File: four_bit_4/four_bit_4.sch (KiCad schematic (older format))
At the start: 1 part, among them P1 DIN_41612_128P

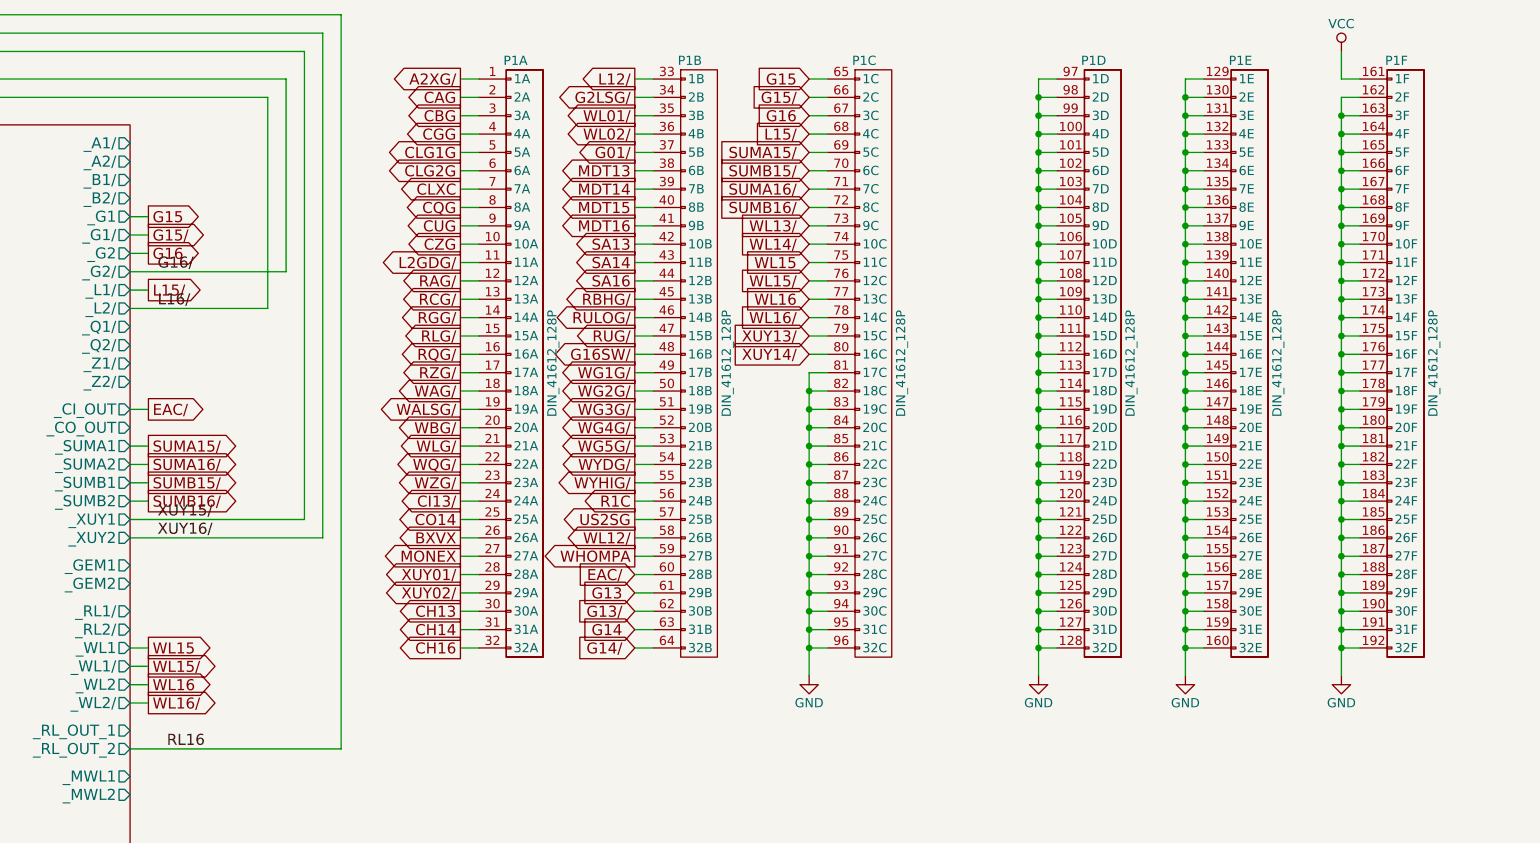
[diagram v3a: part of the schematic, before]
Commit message: Corrected a couple of bugs found by Quartus (L16/, Z15/, Z16/ not connected)
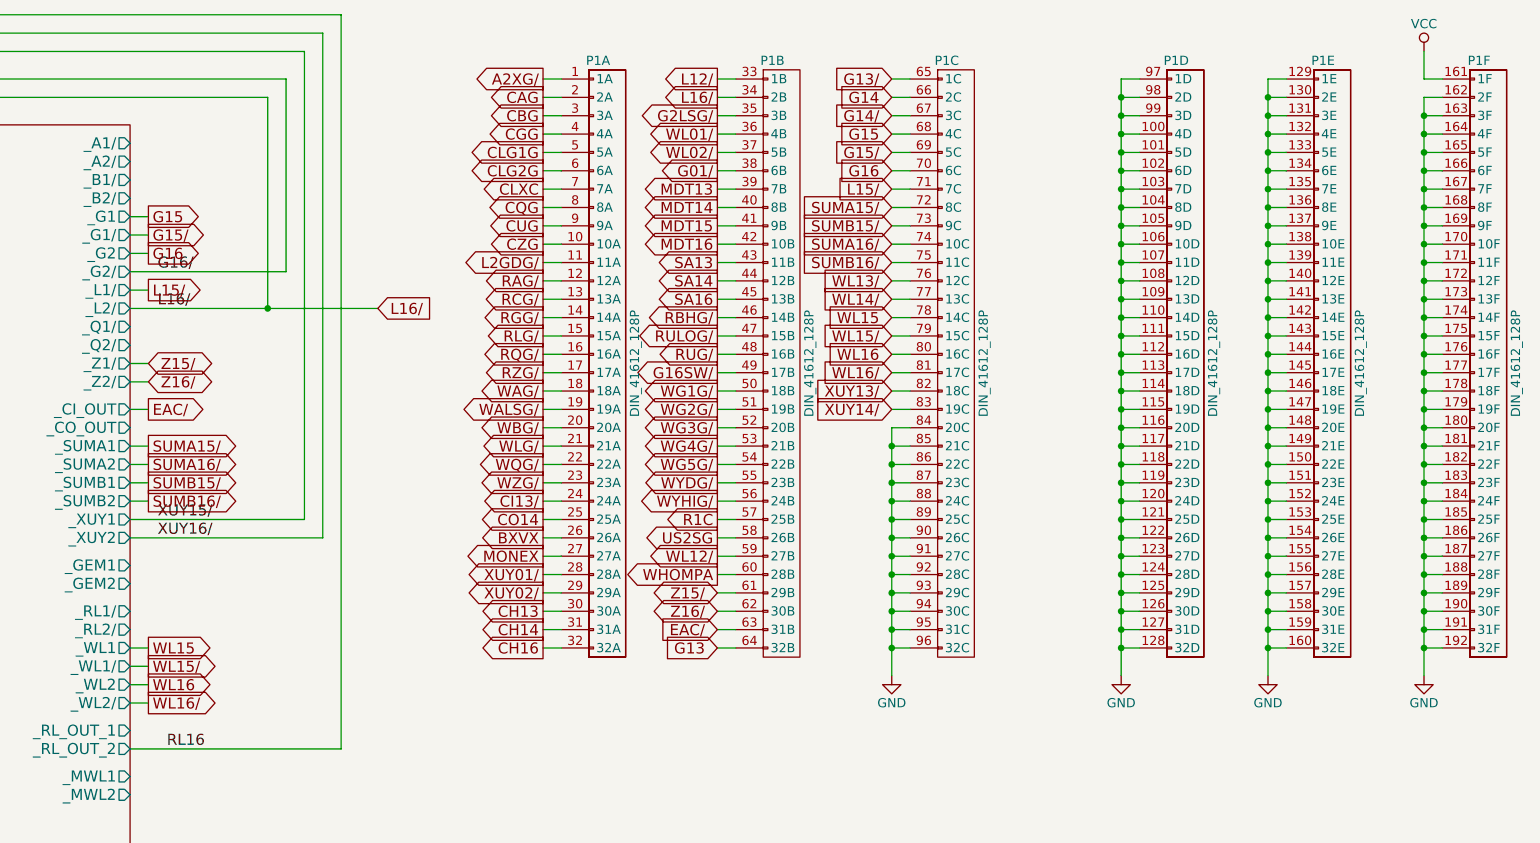
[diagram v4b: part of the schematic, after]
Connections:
- net EAC/: now also P1.63 (31B); no longer P1.60 (28B)
- net G01/: now also P1.38 (6B); no longer P1.37 (5B)
- net G13: now also P1.64 (32B); no longer P1.61 (29B)
- net G13/: now also P1.65 (1C); no longer P1.62 (30B)
- net G14: now also P1.66 (2C); no longer P1.63 (31B)
- net G14/: now also P1.67 (3C); no longer P1.64 (32B)
- net G15: now also P1.68 (4C); no longer P1.65 (1C)
- net G15/: now also P1.69 (5C); no longer P1.66 (2C)
- net G16: now also P1.70 (6C); no longer P1.67 (3C)
- net G16SW/: now also P1.49 (17B); no longer P1.48 (16B)
- net G2LSG/: now also P1.35 (3B); no longer P1.34 (2B)
- net GND: no longer P1.81 (17C), P1.82 (18C), P1.83 (19C)
- net L15/: now also P1.71 (7C); no longer P1.68 (4C)
- net L16/: now also P1.34 (2B)
- net MDT13: now also P1.39 (7B); no longer P1.38 (6B)
- net MDT14: now also P1.40 (8B); no longer P1.39 (7B)
- net MDT15: now also P1.41 (9B); no longer P1.40 (8B)
- net MDT16: now also P1.42 (10B); no longer P1.41 (9B)
- net R1C: now also P1.57 (25B); no longer P1.56 (24B)
- net RBHG/: now also P1.46 (14B); no longer P1.45 (13B)
- net RUG/: now also P1.48 (16B); no longer P1.47 (15B)
- net RULOG/: now also P1.47 (15B); no longer P1.46 (14B)
- net SA13: now also P1.43 (11B); no longer P1.42 (10B)
- net SA14: now also P1.44 (12B); no longer P1.43 (11B)
- net SA16: now also P1.45 (13B); no longer P1.44 (12B)
- net SUMA15/: now also P1.72 (8C); no longer P1.69 (5C)
- net SUMA16/: now also P1.74 (10C); no longer P1.71 (7C)
- net SUMB15/: now also P1.73 (9C); no longer P1.70 (6C)
- net SUMB16/: now also P1.75 (11C); no longer P1.72 (8C)
- net US2SG: now also P1.58 (26B); no longer P1.57 (25B)
- net WG1G/: now also P1.50 (18B); no longer P1.49 (17B)
- net WG2G/: now also P1.51 (19B); no longer P1.50 (18B)
- net WG3G/: now also P1.52 (20B); no longer P1.51 (19B)
- net WG4G/: now also P1.53 (21B); no longer P1.52 (20B)
- net WG5G/: now also P1.54 (22B); no longer P1.53 (21B)
- net WHOMPA: now also P1.60 (28B); no longer P1.59 (27B)
- net WL01/: now also P1.36 (4B); no longer P1.35 (3B)
- net WL02/: now also P1.37 (5B); no longer P1.36 (4B)
- net WL12/: now also P1.59 (27B); no longer P1.58 (26B)
- net WL13/: now also P1.76 (12C); no longer P1.73 (9C)
- net WL14/: now also P1.77 (13C); no longer P1.74 (10C)
- net WL15: now also P1.78 (14C); no longer P1.75 (11C)
- net WL15/: now also P1.79 (15C); no longer P1.76 (12C)
- net WL16: now also P1.80 (16C); no longer P1.77 (13C)
- net WL16/: now also P1.81 (17C); no longer P1.78 (14C)
- net WYDG/: now also P1.55 (23B); no longer P1.54 (22B)
- net WYHIG/: now also P1.56 (24B); no longer P1.55 (23B)
- net XUY13/: now also P1.82 (18C); no longer P1.79 (15C)
- net XUY14/: now also P1.83 (19C); no longer P1.80 (16C)
- new net Z15/: P1.61 (29B)
- new net Z16/: P1.62 (30B)
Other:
- moved on the sheet: P1A, P1B, P1C, P1D, P1E, P1F

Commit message: Added and tied in module 15, the rupt service (and banking/rope+strand selection)
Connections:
- net GND: no longer P1.84 (20C), P1.85 (21C), P1.86 (22C), P1.87 (23C), P1.88 (24C), P1.89 (25C), P1.90 (26C), P1.91 (27C)
- net SUMA15/: now also P1.80 (16C); no longer P1.72 (8C)
- net SUMA16/: now also P1.82 (18C); no longer P1.74 (10C)
- net SUMB15/: now also P1.81 (17C); no longer P1.73 (9C)
- net SUMB16/: now also P1.83 (19C); no longer P1.75 (11C)
- net WL13/: now also P1.84 (20C); no longer P1.76 (12C)
- net WL14/: now also P1.85 (21C); no longer P1.77 (13C)
- net WL15: now also P1.86 (22C); no longer P1.78 (14C)
- net WL15/: now also P1.87 (23C); no longer P1.79 (15C)
- net WL16: now also P1.88 (24C); no longer P1.80 (16C)
- net WL16/: now also P1.89 (25C); no longer P1.81 (17C)
- net XUY13/: now also P1.90 (26C); no longer P1.82 (18C)
- net XUY14/: now also P1.91 (27C); no longer P1.83 (19C)
- new net RL13/: P1.72 (8C)
- new net RL14/: P1.73 (9C)
- new net RL15/: P1.74 (10C)
- new net RL16/: P1.75 (11C)
- new net SUMA13/: P1.76 (12C)
- new net SUMA14/: P1.78 (14C)
- new net SUMB13/: P1.77 (13C)
- new net SUMB14/: P1.79 (15C)
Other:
- moved on the sheet: P1C
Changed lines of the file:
@@
 L DIN_41612_128P P1
 U 3 1 568CD52A
-P 10450 2500
-F 0 "P1" H 10450 4150 50  0000 C CNN
-F 1 "DIN_41612_128P" V 10650 2500 50  0000 C CNN
-F 2 "" H 10450 2500 60  0000 C CNN
-F 3 "" H 10450 2500 60  0000 C CNN
-	3    10450 2500
+P 10550 2500
+F 0 "P1" H 10550 4150 50  0000 C CNN
+F 1 "DIN_41612_128P" V 10750 2500 50  0000 C CNN
+F 2 "" H 10550 2500 60  0000 C CNN
+F 3 "" H 10550 2500 60  0000 C CNN
+	3    10550 2500
 	1    0    0    -1
 $EndComp
@@
 L GND #PWR07
 U 1 1 568CD535
-P 10150 4200
-F 0 "#PWR07" H 10150 3950 50  0001 C CNN
-F 1 "GND" H 10150 4050 50  0000 C CNN
-F 2 "" H 10150 4200 60  0000 C CNN
-F 3 "" H 10150 4200 60  0000 C CNN
-	1    10150 4200
+P 10250 4200
+F 0 "#PWR07" H 10250 3950 50  0001 C CNN
+F 1 "GND" H 10250 4050 50  0000 C CNN
+F 2 "" H 10250 4200 60  0000 C CNN
+F 3 "" H 10250 4200 60  0000 C CNN
+	1    10250 4200
 	1    0    0    -1
 $EndComp
@@
 	4600 8350 4500 8350
 Wire Wire Line
-	10150 2850 10250 2850
-Wire Wire Line
-	10150 2950 10250 2950
-Connection ~ 10150 2950
-Wire Wire Line
-	10150 3050 10250 3050
-Connection ~ 10150 3050
-Wire Wire Line
-	10150 3150 10250 3150
-Connection ~ 10150 3150
-Wire Wire Line
-	10150 3250 10250 3250
-Connection ~ 10150 3250
-Wire Wire Line
-	10150 3350 10250 3350
-Connection ~ 10150 3350
-Wire Wire Line
-	10150 3450 10250 3450
-Connection ~ 10150 3450
-Wire Wire Line
-	10150 3550 10250 3550
-Connection ~ 10150 3550
-Wire Wire Line
-	10150 3650 10250 3650
-Connection ~ 10150 3650
-Wire Wire Line
-	10150 3750 10250 3750
-Connection ~ 10150 3750
-Wire Wire Line
-	10150 3850 10250 3850
-Connection ~ 10150 3850
-Wire Wire Line
-	10150 3950 10250 3950
-Connection ~ 10150 3950
-Wire Wire Line
-	10150 4050 10250 4050
-Connection ~ 10150 4050
+	10250 3650 10350 3650
+Wire Wire Line
+	10250 3750 10350 3750
+Connection ~ 10250 3750
+Wire Wire Line
+	10250 3850 10350 3850
+Connection ~ 10250 3850
+Wire Wire Line
+	10250 3950 10350 3950
+Connection ~ 10250 3950
+Wire Wire Line
+	10250 4050 10350 4050
+Connection ~ 10250 4050
 Wire Wire Line
 	6000 2000 6850 2000
@@
 Wire Wire Line
 	6000 1800 6100 1800
-Text GLabel 10150 950  0    60   Input ~ 0
+Text GLabel 10250 950  0    60   Input ~ 0
 G13/
 Wire Wire Line
-	10250 950  10150 950
-Text GLabel 10150 1150 0    60   Input ~ 0
+	10350 950  10250 950
+Text GLabel 10250 1150 0    60   Input ~ 0
 G14/
 Wire Wire Line
-	10250 1150 10150 1150
-Text GLabel 10150 1350 0    60   Input ~ 0
+	10350 1150 10250 1150
+Text GLabel 10250 1350 0    60   Input ~ 0
 G15/
 Wire Wire Line
-	10250 1350 10150 1350
+	10350 1350 10250 1350
 Text GLabel 6100 2100 2    60   Output ~ 0
 L15/
 Wire Wire Line
 	6000 2100 6100 2100
-Text GLabel 10150 1550 0    60   Input ~ 0
+Text GLabel 10250 1550 0    60   Input ~ 0
 L15/
 Wire Wire Line
-	10250 1550 10150 1550
+	10350 1550 10250 1550
 Text GLabel 6100 3050 2    60   Output ~ 0
 SUMA16/
@@
 Wire Wire Line
 	6000 3250 6100 3250
-Text GLabel 10150 1850 0    60   Input ~ 0
+Text GLabel 10250 2650 0    60   Input ~ 0
 SUMA16/
 Wire Wire Line
-	10250 1850 10150 1850
-Text GLabel 10150 1950 0    60   Input ~ 0
+	10350 2650 10250 2650
+Text GLabel 10250 2750 0    60   Input ~ 0
 SUMB16/
 Wire Wire Line
-	10250 1950 10150 1950
+	10350 2750 10250 2750
 Text GLabel 3250 3350 2    60   Output ~ 0
 XUY13/
@@
 Wire Wire Line
 	3150 3450 3250 3450
-Text GLabel 10150 2650 0    60   Input ~ 0
+Text GLabel 10250 3450 0    60   Input ~ 0
 XUY13/
 Wire Wire Line
-	10250 2650 10150 2650
-Text GLabel 10150 2750 0    60   Input ~ 0
+	10350 3450 10250 3450
+Text GLabel 10250 3550 0    60   Input ~ 0
 XUY14/
 Wire Wire Line
-	10250 2750 10150 2750
+	10350 3550 10250 3550
 Text GLabel 6100 4050 2    60   Output ~ 0
 WL15
@@
 Wire Wire Line
 	6000 4250 6100 4250
-Text GLabel 10150 2050 0    60   Input ~ 0
+Text GLabel 10250 2850 0    60   Input ~ 0
 WL13/
-Text GLabel 10150 2150 0    60   Input ~ 0
+Text GLabel 10250 2950 0    60   Input ~ 0
 WL14/
 Wire Wire Line
-	10250 2050 10150 2050
-Wire Wire Line
-	10250 2150 10150 2150
-Text GLabel 10150 2350 0    60   Input ~ 0
+	10350 2850 10250 2850
+Wire Wire Line
+	10350 2950 10250 2950
+Text GLabel 10250 3150 0    60   Input ~ 0
 WL15/
 Wire Wire Line
-	10250 2350 10150 2350
-Wire Wire Line
-	10250 2550 10150 2550
-Text GLabel 10150 2250 0    60   Input ~ 0
+	10350 3150 10250 3150
+Wire Wire Line
+	10350 3350 10250 3350
+Text GLabel 10250 3050 0    60   Input ~ 0
 WL15
-Text GLabel 10150 2450 0    60   Input ~ 0
+Text GLabel 10250 3250 0    60   Input ~ 0
 WL16
 Wire Wire Line
-	10250 2250 10150 2250
-Wire Wire Line
-	10250 2450 10150 2450
-Text GLabel 10150 2550 0    60   Input ~ 0
+	10350 3050 10250 3050
+Wire Wire Line
+	10350 3250 10250 3250
+Text GLabel 10250 3350 0    60   Input ~ 0
 WL16/
 Text GLabel 6100 2750 2    60   Output ~ 0
@@
 Wire Wire Line
 	6000 2950 6100 2950
-Text GLabel 10150 1650 0    60   Input ~ 0
+Text GLabel 10250 2450 0    60   Input ~ 0
 SUMA15/
 Wire Wire Line
-	10250 1650 10150 1650
-Text GLabel 10150 1750 0    60   Input ~ 0
+	10350 2450 10250 2450
+Text GLabel 10250 2550 0    60   Input ~ 0
 SUMB15/
 Wire Wire Line
-	10250 1750 10150 1750
+	10350 2550 10250 2550
 $Comp
 L GND #PWR014
@@
 Wire Wire Line
 	9300 4050 9200 4050
-Text GLabel 10150 1050 0    60   Input ~ 0
+Text GLabel 10250 1050 0    60   Input ~ 0
 G14
 Wire Wire Line
-	10250 1050 10150 1050
-Text GLabel 10150 1250 0    60   Input ~ 0
+	10350 1050 10250 1050
+Text GLabel 10250 1250 0    60   Input ~ 0
 G15
 Wire Wire Line
-	10250 1250 10150 1250
-Text GLabel 10150 1450 0    60   Input ~ 0
+	10350 1250 10250 1250
+Text GLabel 10250 1450 0    60   Input ~ 0
 G16
 Wire Wire Line
-	10250 1450 10150 1450
+	10350 1450 10250 1450
 Text GLabel 7350 2200 2    60   Input ~ 0
 L16/
@@
 Wire Wire Line
 	6000 2500 6100 2500
-Wire Wire Line
-	10150 2850 10150 4200
 Text GLabel 9200 3750 0    60   BiDi ~ 0
 Z15/
@@
 Wire Wire Line
 	9300 3850 9200 3850
+Text GLabel 3250 2950 2    60   Output ~ 0
+SUMA13/
+Wire Wire Line
+	3150 2950 3250 2950
+Text GLabel 3250 3050 2    60   Output ~ 0
+SUMA14/
+Wire Wire Line
+	3150 3050 3250 3050
+Text GLabel 3250 3150 2    60   Output ~ 0
+SUMB13/
+Wire Wire Line
+	3150 3150 3250 3150
+Text GLabel 3250 3250 2    60   Output ~ 0
+SUMB14/
+Wire Wire Line
+	3150 3250 3250 3250
+Text GLabel 10250 2050 0    60   Input ~ 0
+SUMA13/
+Wire Wire Line
+	10350 2050 10250 2050
+Text GLabel 10250 2250 0    60   Input ~ 0
+SUMA14/
+Wire Wire Line
+	10350 2250 10250 2250
+Text GLabel 10250 2150 0    60   Input ~ 0
+SUMB13/
+Wire Wire Line
+	10350 2150 10250 2150
+Text GLabel 10250 2350 0    60   Input ~ 0
+SUMB14/
+Wire Wire Line
+	10350 2350 10250 2350
+Text GLabel 3250 3850 2    60   BiDi ~ 0
+RL13/
+Wire Wire Line
+	3150 3850 3250 3850
+Text GLabel 3250 3950 2    60   BiDi ~ 0
+RL14/
+Wire Wire Line
+	3150 3950 3250 3950
+Text GLabel 6100 3850 2    60   BiDi ~ 0
+RL15/
+Wire Wire Line
+	6000 3850 6100 3850
+Text GLabel 6100 3950 2    60   BiDi ~ 0
+RL16/
+Wire Wire Line
+	6000 3950 6100 3950
+Text GLabel 10250 1650 0    60   BiDi ~ 0
+RL13/
+Wire Wire Line
+	10350 1650 10250 1650
+Text GLabel 10250 1750 0    60   BiDi ~ 0
+RL14/
+Wire Wire Line
+	10350 1750 10250 1750
+Text GLabel 10250 1850 0    60   BiDi ~ 0
+RL15/
+Wire Wire Line
+	10350 1850 10250 1850
+Text GLabel 10250 1950 0    60   BiDi ~ 0
+RL16/
+Wire Wire Line
+	10350 1950 10250 1950
+Wire Wire Line
+	10250 3650 10250 4200
 $EndSCHEMATC

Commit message: Added erasable memory, and fixed lots of random wiring errors.
I decided to go with a 16-bit-wide MRAM chip -- I had  no idea
until I started researching RAM options how technologically
similar MRAM is to core memory. The datasheet diagrams look like
they're straight out of the AGC documentation!

There's a slight inaccuracy in this implementation worth mentioning.
Like fixed memory, I've wired the sense amplifier outputs directly up
to the tristate data output pins of the MRAM chip. But because the
data lines are bidirectional, data being written into RAM will show up
on the sense lines, and go straight into the ungated G register. Since
G is what's being written out, this doesn't matter 99% of the time, but
if there's an overflow condition in G (I don't even know if this is
possible), the bit 16 will be copied over bit 16, and the overflow
condition will be lost. I'll keep an eye out to see if anything relies
on G not changing after the write cycle is complete.

With erasable memory introduced, the computer now theoretically supports
all programs that don't use I/O or interrupts. I've started running
the VirtualAGC validation program, and have been fixing random errors
uncovered by failing self-tests.
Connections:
- net GND: no longer P1.92 (28C), P1.93 (29C), P1.94 (30C)
- new net GEM13: P1.92 (28C)
- new net GEM14: P1.93 (29C)
- new net GEM16: P1.94 (30C)
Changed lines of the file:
@@
 	4600 8350 4500 8350
 Wire Wire Line
-	10250 3650 10350 3650
-Wire Wire Line
-	10250 3750 10350 3750
-Connection ~ 10250 3750
-Wire Wire Line
-	10250 3850 10350 3850
-Connection ~ 10250 3850
-Wire Wire Line
 	10250 3950 10350 3950
-Connection ~ 10250 3950
 Wire Wire Line
 	10250 4050 10350 4050
@@
 Wire Wire Line
 	10350 1950 10250 1950
-Wire Wire Line
-	10250 3650 10250 4200
+Text GLabel 3250 3600 2    60   Output ~ 0
+GEM13
+Wire Wire Line
+	3150 3600 3250 3600
+Text GLabel 3250 3700 2    60   Output ~ 0
+GEM14
+Wire Wire Line
+	3150 3700 3250 3700
+Text GLabel 6100 3700 2    60   Output ~ 0
+GEM16
+Wire Wire Line
+	6000 3700 6100 3700
+Wire Wire Line
+	10250 3950 10250 4200
+Text GLabel 10250 3750 0    60   Input ~ 0
+GEM14
+Wire Wire Line
+	10350 3750 10250 3750
+Text GLabel 10250 3850 0    60   Input ~ 0
+GEM16
+Wire Wire Line
+	10350 3850 10250 3850
+Wire Wire Line
+	10350 3650 10250 3650
+Text GLabel 10250 3650 0    60   Input ~ 0
+GEM13
 $EndSCHEMATC
